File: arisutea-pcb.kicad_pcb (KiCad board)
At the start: 2 copper layers, 339.1 x 121 mm, 179 parts, among them J10 PF6, J11 PF7, J12 VCC, J13 D+, J14 D-, J15 GND, J2 MISO, J3 VCC, J4 SCK, J5 MOSI, J6 RES, J7 GND, J8 PF4, J9 PF5, SW1 SW_Push, SW10 SW_Push, SW11 SW_Push, SW12 SW_Push, SW13 SW_Push, SW14 SW_Push, SW15 SW_Push, SW16 SW_Push, SW17 SW_Push, SW18 SW_Push, SW19 SW_Push, SW2 SW_Push, SW20 SW_Push, SW21 SW_Push, SW22 SW_Push, SW23 SW_Push, SW24 SW_Push, SW25 SW_Push, SW26 SW_Push, SW27 SW_Push, SW28 SW_Push, SW29 SW_Push, SW3 SW_Push, SW30 SW_Push, SW31 SW_Push, SW32 SW_Push, SW33 SW_Push, SW34 SW_Push, SW35 SW_Push, SW36 SW_Push, SW37 SW_Push, SW38 SW_Push, SW39 SW_Push, SW4 SW_Push, SW40 SW_Push, SW41 SW_Push, SW42 SW_Push, SW43 SW_Push, SW44 SW_Push, SW45 SW_Push, SW46 SW_Push, SW47 SW_Push, SW48 SW_Push, SW49 SW_Push, SW5 SW_Push, SW50 SW_Push, SW51 SW_Push, SW52 SW_Push, SW53 SW_Push, SW54 SW_Push, SW55 SW_Push, SW56 SW_Push, SW57 SW_Push, SW58 SW_Push, SW59 SW_Push, SW6 SW_Push, SW60 SW_Push, SW61 SW_Push, SW62 SW_Push, SW63 SW_Push, SW64 SW_Push, SW65 SW_Push, SW66 SW_Push, SW7 SW_Push, SW8 SW_Push, SW9 SW_Push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

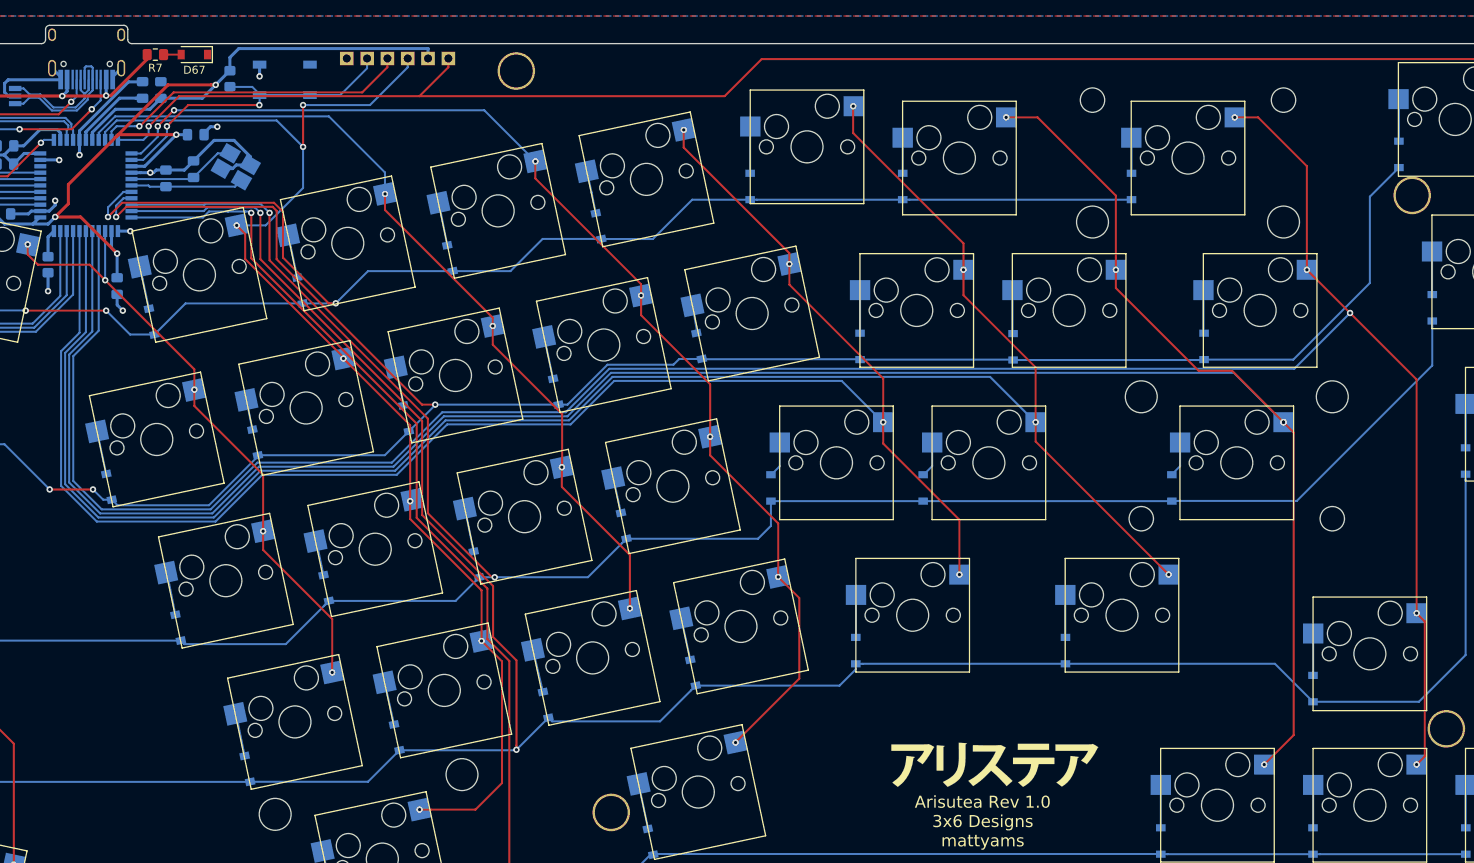
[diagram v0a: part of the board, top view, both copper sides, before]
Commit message: fixed silly routing mistake
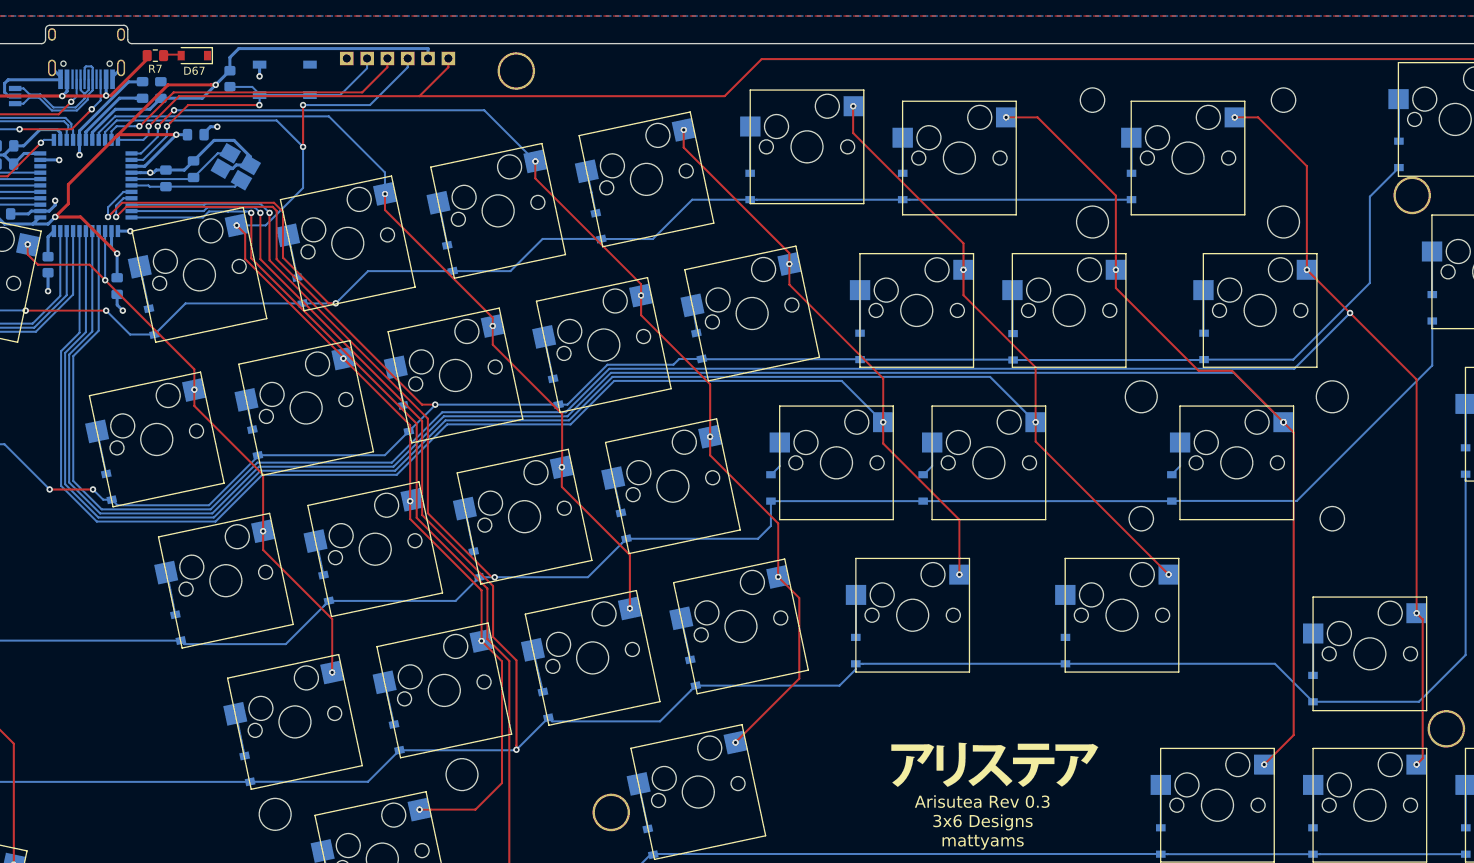
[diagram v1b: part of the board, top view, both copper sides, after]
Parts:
- moved D67 0.13 mm to (189.0, 25.9)
- moved R7 0.13 mm to (184.1, 25.9)
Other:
- board text added: "Arisutea Rev 0.3 3x6 Designs mattyams"
- board text removed: "Arisutea Rev 1.0 3x6 Designs mattyams"

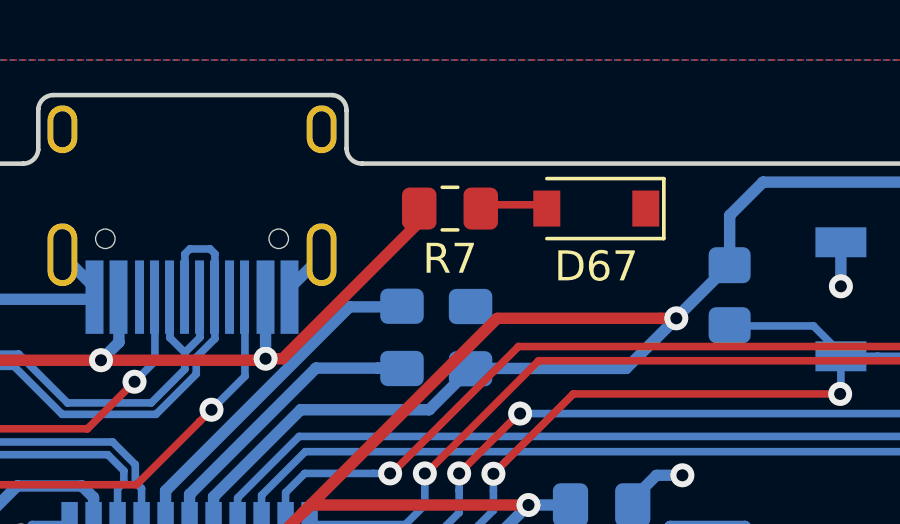
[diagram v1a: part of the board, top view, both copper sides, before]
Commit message: house keeping, fixed another silly routing mistake, regen gerbs and BOM
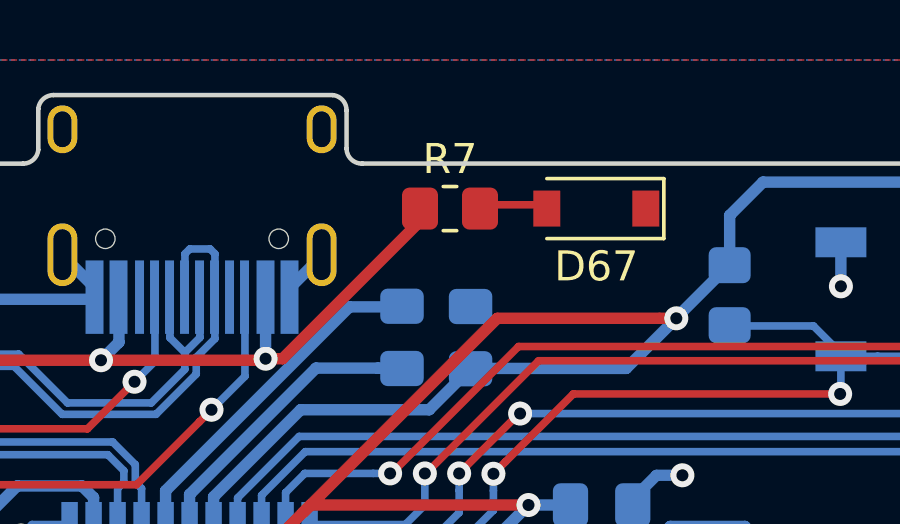
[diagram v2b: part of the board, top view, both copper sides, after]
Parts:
- R7: footprint Resistor_SMD:R_0805_2012Metric_Pad1.15x1.40mm_HandSolder -> Resistor_SMD:R_0805_2012Metric_Pad1.20x1.40mm_HandSolder

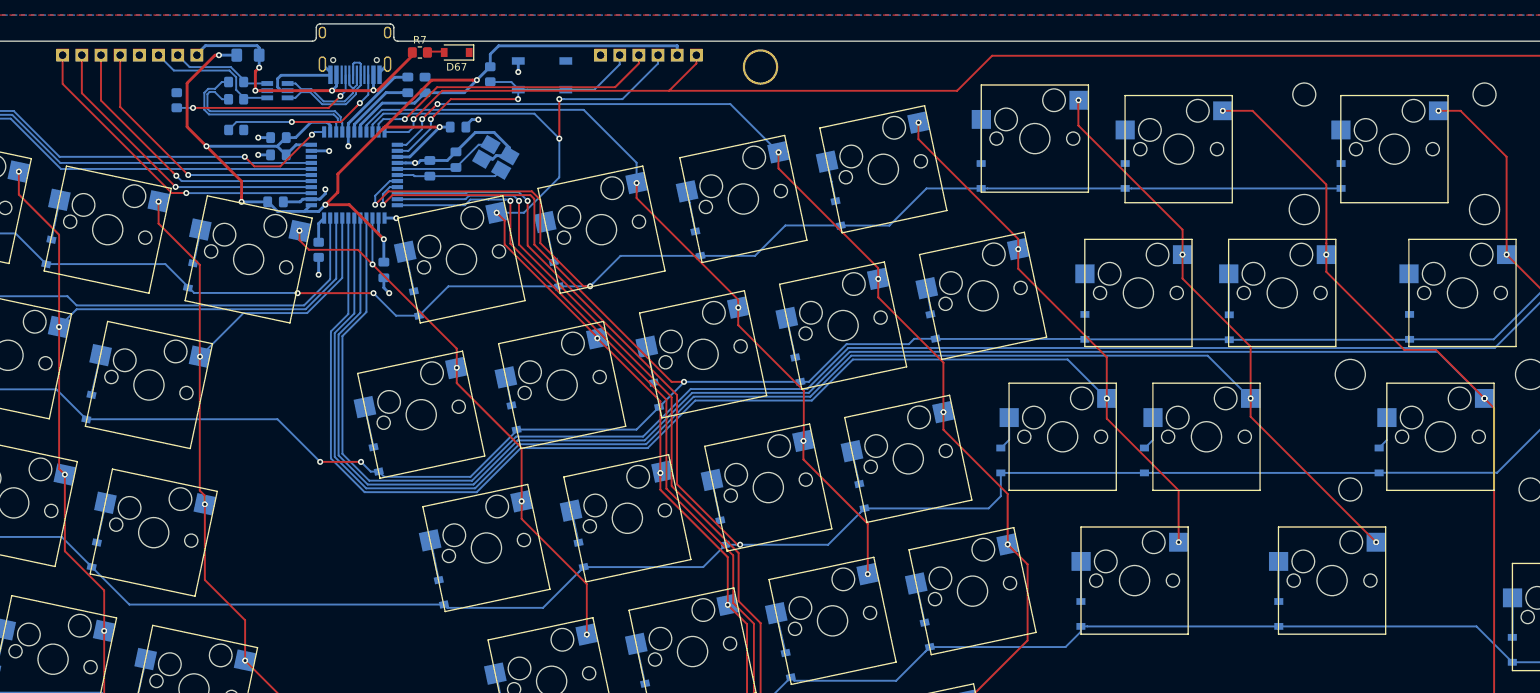
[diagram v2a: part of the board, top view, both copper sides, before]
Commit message: footprint and trace cleanup
Changed some footprints to show clearer positioning of U1, U2 and Y1 as well as all the key switch diodes on the silkscreen.

Correct footprint and name for LED.

Moved a couple of traces around slightly for aesthetics.

Removed some trace tails that were just hanging out.
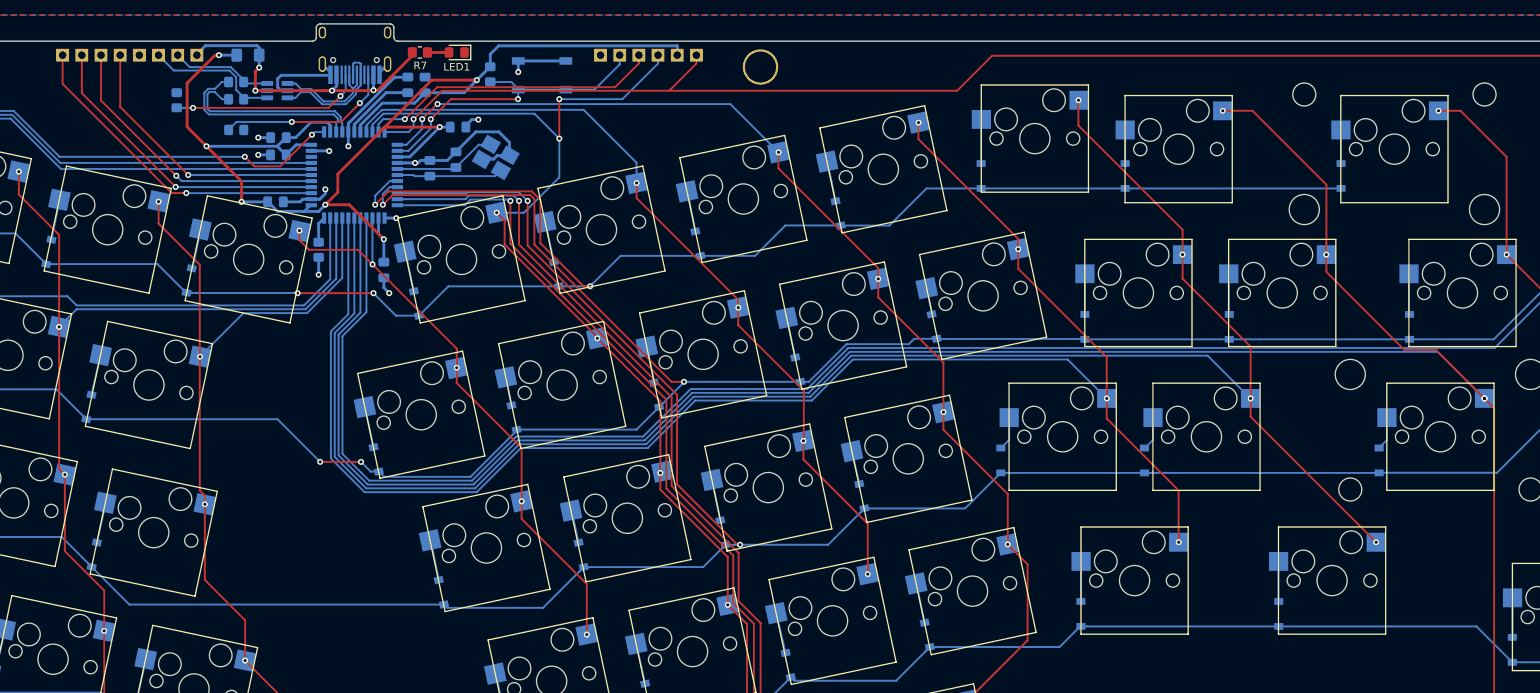
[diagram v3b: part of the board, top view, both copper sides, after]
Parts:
- removed D67: LED, Diode_SMD:D_SOD-123
- added LED1: LED, LED_SMD:LED_0805_2012Metric_Pad1.15x1.40mm_HandSolder, F.Cu at (189.0, 25.9)
- Y1: footprint Crystal:Crystal_SMD_SeikoEpson_FA238-4Pin_3.2x2.5mm_HandSoldering -> Crystal:Crystal_SMD_TXC_7M-4Pin_3.2x2.5mm_HandSoldering
- moved D29 0.68 mm to (153.5, 56.1)
- moved D48 0.15 mm to (252.2, 62.2)
- moved D56 0.05 mm to (291.3, 62.3)
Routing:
- net GND: track 70.9 -> 77.9 mm
- net /row2: track 408.6 -> 406.8 mm
- net Net-(D67-Pad2): track 2.20 -> 2.85 mm
- net Net-(D29-Pad2): track 4.65 -> 5.21 mm
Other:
- rule pad_to_mask_clearance: 0 -> 0.05

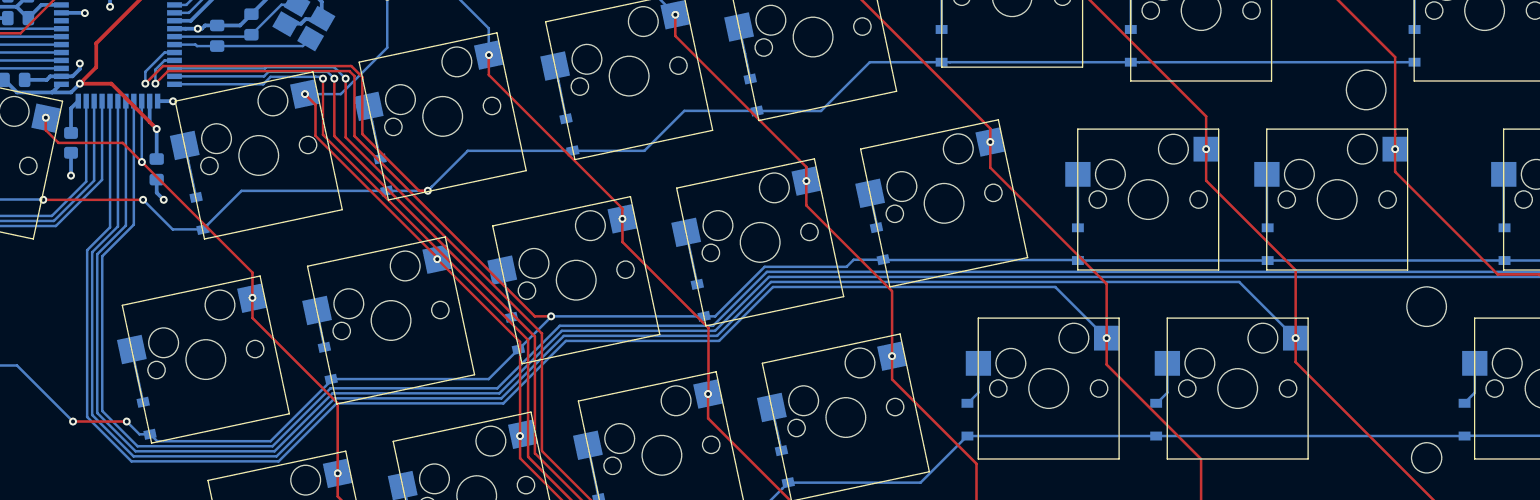
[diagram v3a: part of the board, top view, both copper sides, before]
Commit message: fix some routing boo boos and added boxed case design
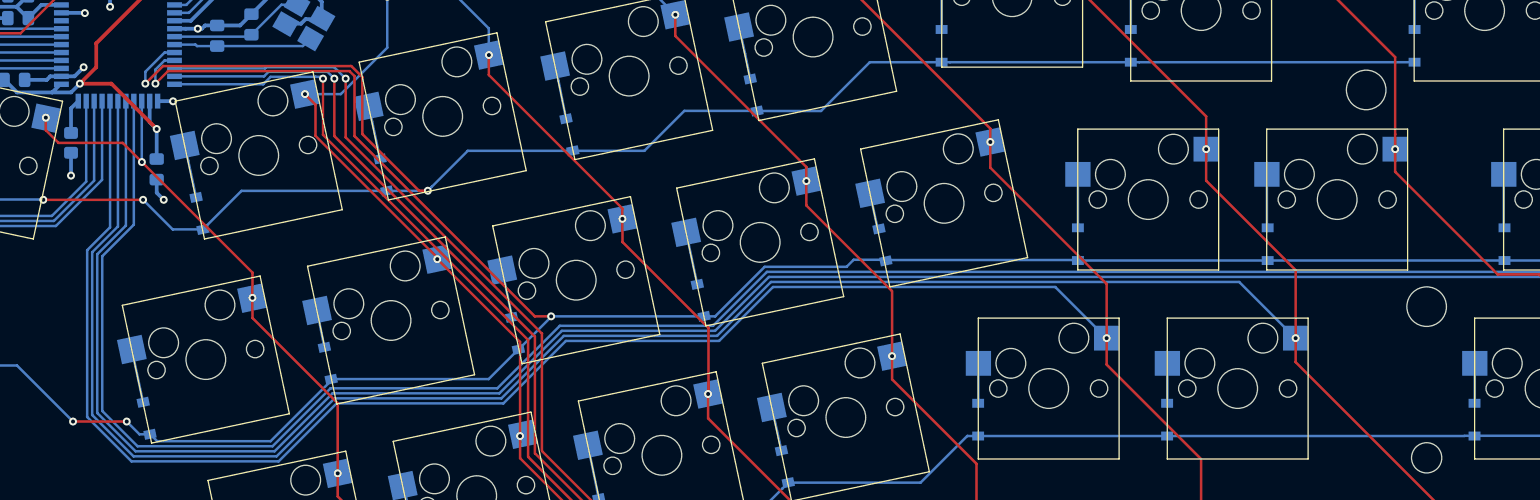
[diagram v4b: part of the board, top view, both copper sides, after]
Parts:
- moved D53 1.10 mm to (281.2, 80.0)
- moved D49 1.08 mm to (262.1, 80.0)
- moved D57 1.00 mm to (312.2, 80.0)
- moved D48 0.28 mm to (252.5, 62.4)
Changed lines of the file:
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@@
   )
   (module Diode_SMD:D_SOD-123 (layer B.Cu)
-    (at 311.1627 79.9719 90)
+    (at 312.166 79.9719 90)
     (descr SOD-123)
     (tags SOD-123)
@@
   )
   (module Diode_SMD:D_SOD-123 (layer B.Cu)
-    (at 280.0731 79.9719 90)
+    (at 281.178 79.9719 90)
     (descr SOD-123)
     (tags SOD-123)
@@
   )
   (module Diode_SMD:D_SOD-123 (layer B.Cu)
-    (at 261.0485 79.9719 90)
+    (at 262.128 79.9719 90)
     (descr SOD-123)
     (tags SOD-123)
@@
   )
   (module Diode_SMD:D_SOD-123 (layer B.Cu)
-    (at 252.222 62.23 102)
+    (at 252.476 62.357 102)
     (descr SOD-123)
     (tags SOD-123)
@@
   (segment (start 174.61875 36.464) (end 174.61875 35.339) (width 0.381) (layer B.Cu) (net 2))
   (segment (start 174.61875 35.339) (end 180.74775 29.21) (width 0.381) (layer B.Cu) (net 2))
-  (via (at 171.577 44.069) (size 0.8) (drill 0.4) (layers F.Cu B.Cu) (net 2))
-  (segment (start 171.577 44.63075) (end 171.577 44.069) (width 0.381) (layer B.Cu) (net 2))
-  (segment (start 169.71875 45.364) (end 170.84375 45.364) (width 0.381) (layer B.Cu) (net 2))
-  (segment (start 170.84375 45.364) (end 171.577 44.63075) (width 0.381) (layer B.Cu) (net 2))
   (via (at 172.084998 38.989) (size 0.8) (drill 0.4) (layers F.Cu B.Cu) (net 2))
   (segment (start 172.059998 38.964) (end 172.084998 38.989) (width 0.375) (layer B.Cu) (net 2))
@@
   (segment (start 170.688 53.213) (end 170.688 55.372) (width 0.381) (layer B.Cu) (net 2))
   (segment (start 197.129 27.056) (end 203.429 27.056) (width 0.381) (layer B.Cu) (net 2))
+  (via (at 171.958 44.45) (size 0.8) (drill 0.4) (layers F.Cu B.Cu) (net 2))
+  (segment (start 169.71875 45.364) (end 171.044 45.364) (width 0.381) (layer B.Cu) (net 2))
+  (segment (start 171.558001 44.849999) (end 171.958 44.45) (width 0.381) (layer B.Cu) (net 2))
+  (segment (start 171.044 45.364) (end 171.558001 44.849999) (width 0.381) (layer B.Cu) (net 2))
   (segment (start 191.894328 38.149572) (end 193.451863 38.149572) (width 0.254) (layer B.Cu) (net 3))
   (segment (start 188.8744 41.1695) (end 191.894328 38.149572) (width 0.254) (layer B.Cu) (net 3))
@@
   (segment (start 251.459822 58.232568) (end 251.240729 57.154559) (width 0.254) (layer B.Cu) (net 58))
   (segment (start 251.968 60.579) (end 251.459822 58.232568) (width 0.254) (layer B.Cu) (net 58))
-  (segment (start 262.155 77.2525) (end 261.112 78.2955) (width 0.25) (layer B.Cu) (net 59))
-  (segment (start 262.155 74.295) (end 262.155 77.2525) (width 0.25) (layer B.Cu) (net 59))
+  (segment (start 262.155 78.332) (end 262.128 78.359) (width 0.25) (layer B.Cu) (net 59))
+  (segment (start 262.155 74.295) (end 262.155 78.332) (width 0.25) (layer B.Cu) (net 59))
   (segment (start 271.68 98.6276) (end 271.653 98.6546) (width 0.25) (layer B.Cu) (net 60))
   (segment (start 271.68 93.345) (end 271.68 98.6276) (width 0.25) (layer B.Cu) (net 60))
@@
   (segment (start 272.188 60.6292) (end 272.1864 60.6308) (width 0.25) (layer B.Cu) (net 62))
   (segment (start 272.188 55.245) (end 272.188 60.6292) (width 0.25) (layer B.Cu) (net 62))
-  (segment (start 281.205 77.2525) (end 280.0985 78.359) (width 0.25) (layer B.Cu) (net 63))
-  (segment (start 281.205 74.295) (end 281.205 77.2525) (width 0.25) (layer B.Cu) (net 63))
+  (segment (start 281.205 78.332) (end 281.178 78.359) (width 0.25) (layer B.Cu) (net 63))
+  (segment (start 281.205 74.295) (end 281.205 78.332) (width 0.25) (layer B.Cu) (net 63))
   (segment (start 297.842 98.6308) (end 297.8658 98.6546) (width 0.25) (layer B.Cu) (net 64))
   (segment (start 297.842 93.345) (end 297.842 98.6308) (width 0.25) (layer B.Cu) (net 64))
@@
   (segment (start 291.238 60.607) (end 291.3126 60.6816) (width 0.25) (layer B.Cu) (net 66))
   (segment (start 291.238 55.245) (end 291.238 60.607) (width 0.25) (layer B.Cu) (net 66))
-  (segment (start 312.193 77.2525) (end 311.15 78.2955) (width 0.25) (layer B.Cu) (net 67))
-  (segment (start 312.193 74.295) (end 312.193 77.2525) (width 0.25) (layer B.Cu) (net 67))
+  (segment (start 312.193 78.332) (end 312.166 78.359) (width 0.25) (layer B.Cu) (net 67))
+  (segment (start 312.193 74.295) (end 312.193 78.332) (width 0.25) (layer B.Cu) (net 67))
   (segment (start 309.78 122.4528) (end 309.7784 122.4544) (width 0.25) (layer B.Cu) (net 68))
   (segment (start 309.78 117.094) (end 309.78 122.4528) (width 0.25) (layer B.Cu) (net 68))
@@
   (segment (start 175.764 30.23) (end 175.764 29.972) (width 0.254) (layer B.Cu) (net 105))
   (segment (start 175.26 30.734) (end 175.764 30.23) (width 0.254) (layer B.Cu) (net 105))
-  (segment (start 167.6298 30.038) (end 166.577 30.038) (width 0.254) (layer B.Cu) (net 105))
-  (segment (start 169.7228 30.7848) (end 168.3766 30.7848) (width 0.254) (layer B.Cu) (net 105))
-  (segment (start 171.3484 32.4104) (end 169.7228 30.7848) (width 0.254) (layer B.Cu) (net 105))
-  (segment (start 168.3766 30.7848) (end 167.6298 30.038) (width 0.254) (layer B.Cu) (net 105))
-  (segment (start 174.1424 32.4104) (end 171.3484 32.4104) (width 0.254) (layer B.Cu) (net 105))
-  (segment (start 175.26 31.2928) (end 174.1424 32.4104) (width 0.254) (layer B.Cu) (net 105))
-  (segment (start 175.26 30.6832) (end 175.26 31.2928) (width 0.254) (layer B.Cu) (net 105))
+  (segment (start 167.6298 30.038) (end 166.577 30.038) (width 0.254) (layer B.Cu) (net 105) (status 1000000))
+  (segment (start 175.26 30.6832) (end 175.26 31.2928) (width 0.254) (layer B.Cu) (net 105) (status 1000000))
+  (segment (start 175.26 31.2928) (end 174.1424 32.4104) (width 0.254) (layer B.Cu) (net 105) (status 1000000))
+  (segment (start 174.1424 32.4104) (end 171.3484 32.4104) (width 0.254) (layer B.Cu) (net 105) (status 1000000))
+  (segment (start 168.3766 30.7848) (end 167.6298 30.038) (width 0.254) (layer B.Cu) (net 105) (status 1000000))
+  (segment (start 171.3484 32.4104) (end 169.7228 30.7848) (width 0.254) (layer B.Cu) (net 105) (status 1000000))
+  (segment (start 169.7228 30.7848) (end 168.3766 30.7848) (width 0.254) (layer B.Cu) (net 105) (status 1000000))
   (via (at 157.48 26.289) (size 0.8) (drill 0.4) (layers F.Cu B.Cu) (net 109))
   (via (at 171.577 46.101) (size 0.8) (drill 0.4) (layers F.Cu B.Cu) (net 109))
